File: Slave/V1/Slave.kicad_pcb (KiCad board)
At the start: 2 copper layers, 519 parts, among them J1301 649002227222, J1701 649002227222, J201 Header_Male_Pin_2.54mm_1X6_,_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, J202 Header_Male_Pin_2.54mm_1X3_,_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, J2101 649002227222, J2501 649002227222, J2901 649002227222, J300 Header_Male_Pin_2.54mm_1X2_,_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, J301 Header_Male_Pin_2.54mm_1X2_,_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, J3301 649002227222, J401 649006227222, J402 649006227222, J501 649002227222, J901 649002227222, Q1201 CPH6347-TL-W, Q1202 BSS806NH6327XTSA1, Q1301 CPH6347-TL-W, Q1302 CPH6347-TL-W, Q1601 CPH6347-TL-W, Q1602 BSS806NH6327XTSA1, Q1701 CPH6347-TL-W, Q1702 CPH6347-TL-W, Q2001 CPH6347-TL-W, Q2002 BSS806NH6327XTSA1, Q2101 CPH6347-TL-W, Q2102 CPH6347-TL-W, Q2401 CPH6347-TL-W, Q2402 BSS806NH6327XTSA1, Q2501 CPH6347-TL-W, Q2502 CPH6347-TL-W, Q2801 CPH6347-TL-W, Q2802 BSS806NH6327XTSA1, Q2901 CPH6347-TL-W, Q2902 CPH6347-TL-W, Q3201 CPH6347-TL-W, Q3202 BSS806NH6327XTSA1, Q3301 CPH6347-TL-W, Q3302 CPH6347-TL-W, Q3601 CPH6347-TL-W, Q3602 BSS806NH6327XTSA1, Q501 CPH6347-TL-W, Q502 CPH6347-TL-W, Q801 CPH6347-TL-W, Q802 BSS806NH6327XTSA1, Q901 CPH6347-TL-W, Q902 CPH6347-TL-W, SW201 PTS645SM43SMTR92, SW202 PTS645SM43SMTR92, U1001 AP3015KTR-G1, U1002 AP2202K-ADJTRG1, U1101 ADC121S021CIMF/NOPB, U1201 ADCMP350YKSZ-REEL7, U1301 LTV-816S, U1302 SI8641AB-B-IS1, U1401 AP3015KTR-G1, U1402 AP2202K-ADJTRG1, U1501 ADC121S021CIMF/NOPB, U1601 ADCMP350YKSZ-REEL7, U1701 LTV-816S, U1702 SI8641AB-B-IS1, U1801 AP3015KTR-G1, U1802 AP2202K-ADJTRG1, U1901 ADC121S021CIMF/NOPB, U2001 ADCMP350YKSZ-REEL7, U201 STM32F446RE, U2101 LTV-816S, U2102 SI8641AB-B-IS1, U2201 AP3015KTR-G1, U2202 AP2202K-ADJTRG1, U2301 ADC121S021CIMF/NOPB, U2401 ADCMP350YKSZ-REEL7, U2501 LTV-816S, U2502 SI8641AB-B-IS1, U2601 AP3015KTR-G1, U2602 AP2202K-ADJTRG1, U2701 ADC121S021CIMF/NOPB, U2801 ADCMP350YKSZ-REEL7, U2901 LTV-816S, U2902 SI8641AB-B-IS1, U3001 AP3015KTR-G1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

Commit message: Routing signals
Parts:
- removed J301: Header_Male_Pin_2.54mm_1X2_,_Unshrouded, Connectors:Headers_2.54mm_1X2
- removed TP201, TP202, TP203, TP302, TP304: Test_Point_THM, Connectors:Keystone_5001
- added F1301: 39511000440, Fuses:TE5_395, F.Cu at (98.8, 93.0)
- added F1701: 39511000440, Fuses:TE5_395, F.Cu at (98.8, 115.1)
- added F2101: 39511000440, Fuses:TE5_395, F.Cu at (208.0, 128.8)
- added F2501: 39511000440, Fuses:TE5_395, F.Cu at (208.0, 106.7)
- added F2901: 39511000440, Fuses:TE5_395, F.Cu at (208.0, 84.6)
- added F3301: 39511000440, Fuses:TE5_395, F.Cu at (208.0, 62.5)
- added F501: 39511000440, Fuses:TE5_395, F.Cu at (98.8, 48.8)
- added F901: 39511000440, Fuses:TE5_395, F.Cu at (98.8, 70.9)
- added J101: 649002227222, Connectors:649002227222, F.Cu at (211.6, 138.7)
- added J102: 649002227222, Connectors:649002227222, F.Cu at (95.5, 138.9)
- added Q101: 2N7002P,215, IC:SOT-23-3, F.Cu at (-0.57, -0.08)
- added R101: RC0805JR-07470RL, Resistors:R0805, F.Cu at (-1.80, -5.84)
- added R405: RC0805JR-07100RL, Resistors:R0805, F.Cu at (193.8, 148.1)
- C203, C204, C207, C208, C209, C210, C211, C212, C213, C301, C302, C303, C304, C404, D401, D402, R203, R204, R301, R302, R303, R402, R403, R404: moved to B.Cu
- C402, C403, C406, C407: value Capacitor_Generic -> 885012007053; moved to B.Cu
- C405: value Capacitor_Generic -> 885012207080
- R1310, R1710, R2110, R2510, R2910, R3310, R510, R910: moved to F.Cu
- R401: value Resistor_Generic -> RC0805JR-07100RL
- moved R401 355.4 mm to (204.7, 146.0), turned to 270 degrees
- moved C406 346.3 mm to (212.9, 165.6), turned to 180 degrees
- moved C407 339.8 mm to (216.7, 159.3), turned to 90 degrees
- moved C405 337.4 mm to (207.3, 146.0), turned to 270 degrees
- moved R303 336.5 mm to (180.1, 169.7), turned to 180 degrees
- moved D303 334.7 mm to (178.0, 169.7)
- moved D402 329.3 mm to (213.1, 152.9), turned to 180 degrees
- moved C402 328.6 mm to (195.6, 159.3), turned to 90 degrees
- moved C404 326.4 mm to (200.7, 145.3), turned to 180 degrees
- moved D302 324.1 mm to (171.2, 154.9), turned to 180 degrees
- moved TP401 321.5 mm to (201.2, 163.3), turned to 270 degrees
- moved C301 320.6 mm to (174.2, 163.8), turned to 270 degrees
- moved TP402 320.1 mm to (205.0, 150.1)
- moved D301 319.8 mm to (176.8, 154.9), turned to 180 degrees
- moved R402 319.7 mm to (201.2, 156.2), turned to 180 degrees
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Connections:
- C1302 pad 1: /Module 3/AVDD -> VDD
- C1302 pad 2: /Module 3/AGND -> DGND
- C1303 pad 1: /Module 3/AGND -> DGND
- C1702 pad 1: /Module 4/AVDD -> VDD
- C1702 pad 2: /Module 4/AGND -> DGND
- C1703 pad 1: /Module 4/AGND -> DGND
- C2102 pad 1: /Module 5/AVDD -> VDD
- C2102 pad 2: /Module 5/AGND -> DGND
- C2103 pad 1: /Module 5/AGND -> DGND
- C2502 pad 1: /Module 6/AVDD -> VDD
- C2502 pad 2: /Module 6/AGND -> DGND
- C2503 pad 1: /Module 6/AGND -> DGND
- C2902 pad 1: /Module 7/AVDD -> VDD
- C2902 pad 2: /Module 7/AGND -> DGND
- C2903 pad 1: /Module 7/AGND -> DGND
- C303 pad 2: Net-(C303-Pad2) -> 5V
- C3302 pad 1: /Module 8/AVDD -> VDD
- C3302 pad 2: /Module 8/AGND -> DGND
- C3303 pad 1: /Module 8/AGND -> DGND
- C502 pad 1: /Module 1/AVDD -> VDD
- C502 pad 2: /Module 1/AGND -> DGND
- C503 pad 1: /Module 1/AGND -> DGND
- C902 pad 1: /Module 2/AVDD -> VDD
- C902 pad 2: /Module 2/AGND -> DGND
- C903 pad 1: /Module 2/AGND -> DGND
- D402 pad 1: /CAN1/CAN_N -> /CAN1/CAN_P
- D402 pad 2: /CAN1/CAN_P -> /CAN1/CAN_N
- J1301 pad 2: /Module 3/CELL+ -> Net-(F1301-Pad1)
- J1701 pad 2: /Module 4/CELL+ -> Net-(F1701-Pad1)
- J2101 pad 2: /Module 5/CELL+ -> Net-(F2101-Pad1)
- J2501 pad 2: /Module 6/CELL+ -> Net-(F2501-Pad1)
- J2901 pad 2: /Module 7/CELL+ -> Net-(F2901-Pad1)
- J300 pad 1: Net-(C303-Pad2) -> 3.3V
- J300 pad 2: 5V -> VDD
- J3301 pad 2: /Module 8/CELL+ -> Net-(F3301-Pad1)
- J501 pad 2: /Module 1/CELL+ -> Net-(F501-Pad1)
- J901 pad 2: /Module 2/CELL+ -> Net-(F901-Pad1)
- R1303 pad 2: /Module 3/PWR_ENABLE -> VDD
- R1304 pad 2: /Module 3/BALANCING_PWM -> /BALANCING_PWM_3
- R1306 pad 2: /Module 3/CS_MCU -> /CS_3
- R1308 pad 2: /Module 3/SCLK_MCU -> /SCLK
- R1310 pad 2: /Module 3/SDATA_MCU -> /MISO
- R1311 pad 2: /Module 3/DATA_ENABLE -> /DATA_ENABLE_3
- R1314 pad 1: /Module 3/AGND -> DGND
- R1703 pad 2: /Module 4/PWR_ENABLE -> VDD
- R1704 pad 2: /Module 4/BALANCING_PWM -> /BALANCING_PWM_4
- R1706 pad 2: /Module 4/CS_MCU -> /CS_4
- R1708 pad 2: /Module 4/SCLK_MCU -> /SCLK
- R1710 pad 2: /Module 4/SDATA_MCU -> /MISO
- R1711 pad 2: /Module 4/DATA_ENABLE -> /DATA_ENABLE_4
- R1714 pad 1: /Module 4/AGND -> DGND
- R2103 pad 2: /Module 5/PWR_ENABLE -> VDD
- R2104 pad 2: /Module 5/BALANCING_PWM -> /BALANCING_PWM_5
- R2106 pad 2: /Module 5/CS_MCU -> /CS_5
- R2108 pad 2: /Module 5/SCLK_MCU -> /SCLK
- R2110 pad 2: /Module 5/SDATA_MCU -> /MISO
- R2111 pad 2: /Module 5/DATA_ENABLE -> /DATA_ENABLE_5
- R2114 pad 1: /Module 5/AGND -> DGND
- R2503 pad 2: /Module 6/PWR_ENABLE -> VDD
- R2504 pad 2: /Module 6/BALANCING_PWM -> /BALANCING_PWM_6
- R2506 pad 2: /Module 6/CS_MCU -> /CS_6
- R2508 pad 2: /Module 6/SCLK_MCU -> /SCLK
- R2510 pad 2: /Module 6/SDATA_MCU -> /MISO
- R2511 pad 2: /Module 6/DATA_ENABLE -> /DATA_ENABLE_6
- R2514 pad 1: /Module 6/AGND -> DGND
- R2903 pad 2: /Module 7/PWR_ENABLE -> VDD
- R2904 pad 2: /Module 7/BALANCING_PWM -> /BALANCING_PWM_7
- R2906 pad 2: /Module 7/CS_MCU -> /CS_7
- R2908 pad 2: /Module 7/SCLK_MCU -> /SCLK
- R2910 pad 2: /Module 7/SDATA_MCU -> /MISO
- R2911 pad 2: /Module 7/DATA_ENABLE -> /DATA_ENABLE_7
- R2914 pad 1: /Module 7/AGND -> DGND
- R302 pad 2: Net-(C303-Pad2) -> 5V
- R3303 pad 2: /Module 8/PWR_ENABLE -> VDD
- R3304 pad 2: /Module 8/BALANCING_PWM -> /BALANCING_PWM_8
- R3306 pad 2: /Module 8/CS_MCU -> /CS_8
- R3308 pad 2: /Module 8/SCLK_MCU -> /SCLK
- R3310 pad 2: /Module 8/SDATA_MCU -> /MISO
- R3311 pad 2: /Module 8/DATA_ENABLE -> /DATA_ENABLE_8
- R3314 pad 1: /Module 8/AGND -> DGND
- R503 pad 2: /Module 1/PWR_ENABLE -> VDD
- R504 pad 2: /Module 1/BALANCING_PWM -> /BALANCING_PWM_1
- R506 pad 2: /Module 1/CS_MCU -> /CS_1
- R508 pad 2: /Module 1/SCLK_MCU -> /SCLK
- R510 pad 2: /Module 1/SDATA_MCU -> /MISO
- R511 pad 2: /Module 1/DATA_ENABLE -> /DATA_ENABLE_1
- R514 pad 1: /Module 1/AGND -> DGND
- R903 pad 2: /Module 2/PWR_ENABLE -> VDD
- R904 pad 2: /Module 2/BALANCING_PWM -> /BALANCING_PWM_2
- R906 pad 2: /Module 2/CS_MCU -> /CS_2
- R908 pad 2: /Module 2/SCLK_MCU -> /SCLK
- R910 pad 2: /Module 2/SDATA_MCU -> /MISO
- R911 pad 2: /Module 2/DATA_ENABLE -> /DATA_ENABLE_2
- R914 pad 1: /Module 2/AGND -> DGND
- U1301 pad 2: /Module 3/AGND -> /PWR_ENABLE
- U1302 pad 1: /Module 3/AVDD -> VDD
- U1302 pad 2: /Module 3/AGND -> DGND
- U1302 pad 8: /Module 3/AGND -> DGND
- U1701 pad 2: /Module 4/AGND -> /PWR_ENABLE
- U1702 pad 1: /Module 4/AVDD -> VDD
- U1702 pad 2: /Module 4/AGND -> DGND
- U1702 pad 8: /Module 4/AGND -> DGND
- U201 pad 10: /PC2 -> /DATA_ENABLE_4
- U201 pad 11: /PC3 -> /CS_4
- U201 pad 28: /PB2 -> /CS_5
- U201 pad 29: /PB10 -> /DATA_ENABLE_5
- U201 pad 33: /PB12 -> /CS_6
- U201 pad 34: /PB13 -> /DATA_ENABLE_6
- U201 pad 35: /PB14 -> /CS_7
- U201 pad 36: /PB15 -> /DATA_ENABLE_7
- U201 pad 37: /PC6 -> /BALANCING_PWM_5
- U201 pad 38: /PC7 -> /BALANCING_PWM_6
- U201 pad 39: /PC8 -> /BALANCING_PWM_7
- U201 pad 40: /PC9 -> /BALANCING_PWM_8
- U201 pad 42: /PA9 -> /DATA_ENABLE_8
- U201 pad 43: /PA10 -> /CS_8
- U201 pad 50: /PA15 -> /DATA_ENABLE_1
- U201 pad 51: /PC10 -> /SCLK
- U201 pad 52: /PC11 -> /MISO
- U201 pad 53: /PC12 -> /CS_1
- U201 pad 54: /PD2 -> /DATA_ENABLE_2
- U201 pad 56: /PB4 -> /CS_2
- U201 pad 57: /PB5 -> /PWR_ENABLE_GPIO
- U201 pad 58: /PB6 -> /BALANCING_PWM_1
- U201 pad 59: /PB7 -> /BALANCING_PWM_2
- U201 pad 61: /PB8 -> /BALANCING_PWM_3
- U201 pad 62: /PB9 -> /BALANCING_PWM_4
- U201 pad 8: /PC0 -> /DATA_ENABLE_3
- U201 pad 9: /PC1 -> /CS_3
- U2101 pad 2: /Module 5/AGND -> /PWR_ENABLE
- U2102 pad 1: /Module 5/AVDD -> VDD
- U2102 pad 2: /Module 5/AGND -> DGND
- U2102 pad 8: /Module 5/AGND -> DGND
- U2501 pad 2: /Module 6/AGND -> /PWR_ENABLE
- U2502 pad 1: /Module 6/AVDD -> VDD
- U2502 pad 2: /Module 6/AGND -> DGND
- U2502 pad 8: /Module 6/AGND -> DGND
- U2901 pad 2: /Module 7/AGND -> /PWR_ENABLE
- U2902 pad 1: /Module 7/AVDD -> VDD
- U2902 pad 2: /Module 7/AGND -> DGND
- U2902 pad 8: /Module 7/AGND -> DGND
- U301 pad 3: Net-(C303-Pad2) -> 5V
- U3301 pad 2: /Module 8/AGND -> /PWR_ENABLE
- U3302 pad 1: /Module 8/AVDD -> VDD
- U3302 pad 2: /Module 8/AGND -> DGND
- U3302 pad 8: /Module 8/AGND -> DGND
- U401 pad 4: /PA11 -> Net-(R405-Pad2)
- U501 pad 2: /Module 1/AGND -> /PWR_ENABLE
- U502 pad 1: /Module 1/AVDD -> VDD
- U502 pad 2: /Module 1/AGND -> DGND
- U502 pad 8: /Module 1/AGND -> DGND
- U901 pad 2: /Module 2/AGND -> /PWR_ENABLE
- U902 pad 1: /Module 2/AVDD -> VDD
- U902 pad 2: /Module 2/AGND -> DGND
- U902 pad 8: /Module 2/AGND -> DGND
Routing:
- net VDD: track 0.00 -> 289.2 mm, vias 0 -> 18
- net DGND: track 0.00 -> 280.9 mm, vias 0 -> 22
- net /SCLK: track 0.00 -> 160.2 mm, vias 0 -> 8
- net /MISO: track 0.00 -> 98.7 mm
- net /PWR_ENABLE: track 0.00 -> 98.2 mm, vias 0 -> 4
- net /DATA_ENABLE_4: track 0.00 -> 97.5 mm, vias 0 -> 2
- net /CS_4: track 0.00 -> 96.9 mm, vias 0 -> 2
- net /BALANCING_PWM_8: track 0.00 -> 83.0 mm, vias 0 -> 1
- net /DATA_ENABLE_1: track 0.00 -> 81.5 mm, vias 0 -> 1
- net /CS_8: track 0.00 -> 81.4 mm
- net /DATA_ENABLE_3: track 0.00 -> 80.7 mm, vias 0 -> 1
- net /BALANCING_PWM_1: track 0.00 -> 79.6 mm, vias 0 -> 1
- net /CS_1: track 0.00 -> 79.4 mm, vias 0 -> 2
- net /DATA_ENABLE_8: track 0.00 -> 77.7 mm, vias 0 -> 1
- net /CS_3: track 0.00 -> 75.6 mm, vias 0 -> 2
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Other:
- net class Default: clearance 0.254 -> 0.2032; trace_width 0.254 -> 0.2032
- rule trace_clearance: 0.254 -> 0.2032
- board text added: "12V"
- board text added: "3.3V"
- board text added: "5V"
- board text added: "DGND"
- board text added: "RESET"
- board text added: "USER"

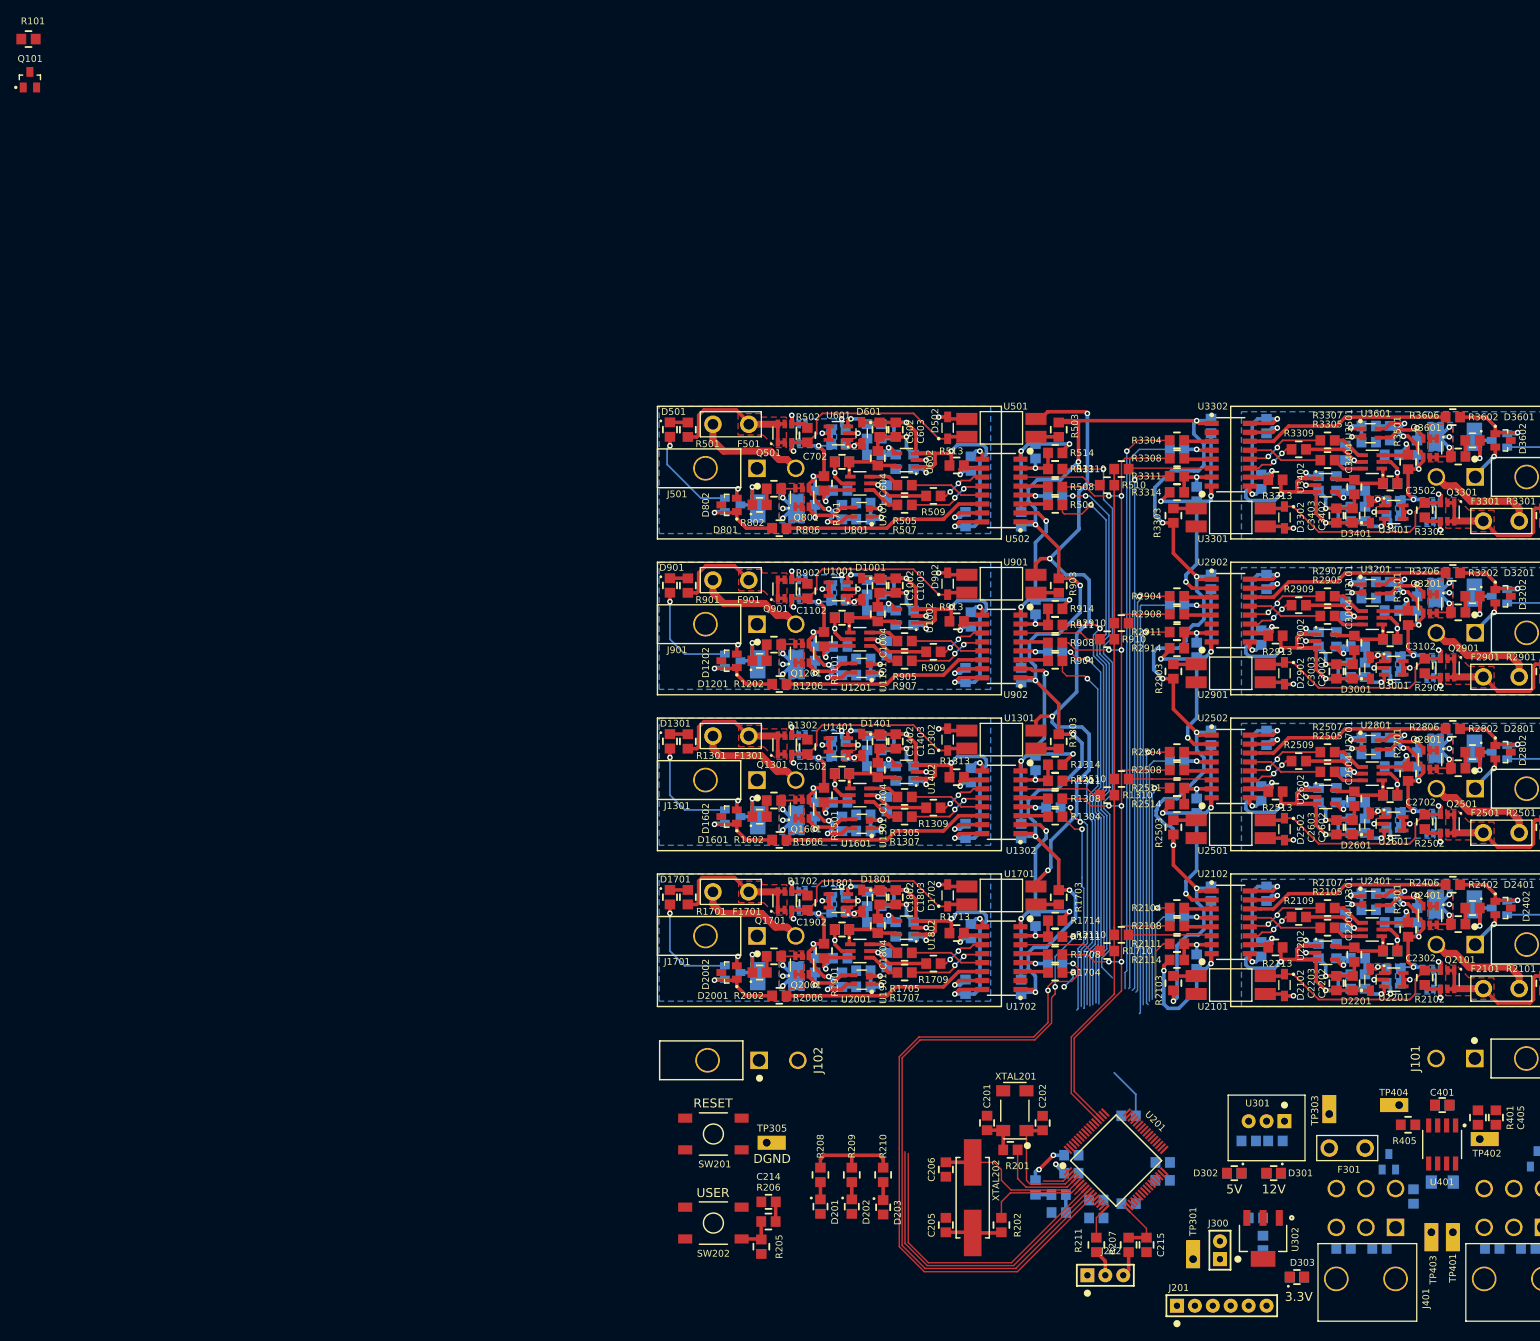
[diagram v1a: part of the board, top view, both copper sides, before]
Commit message: Routing signals 2
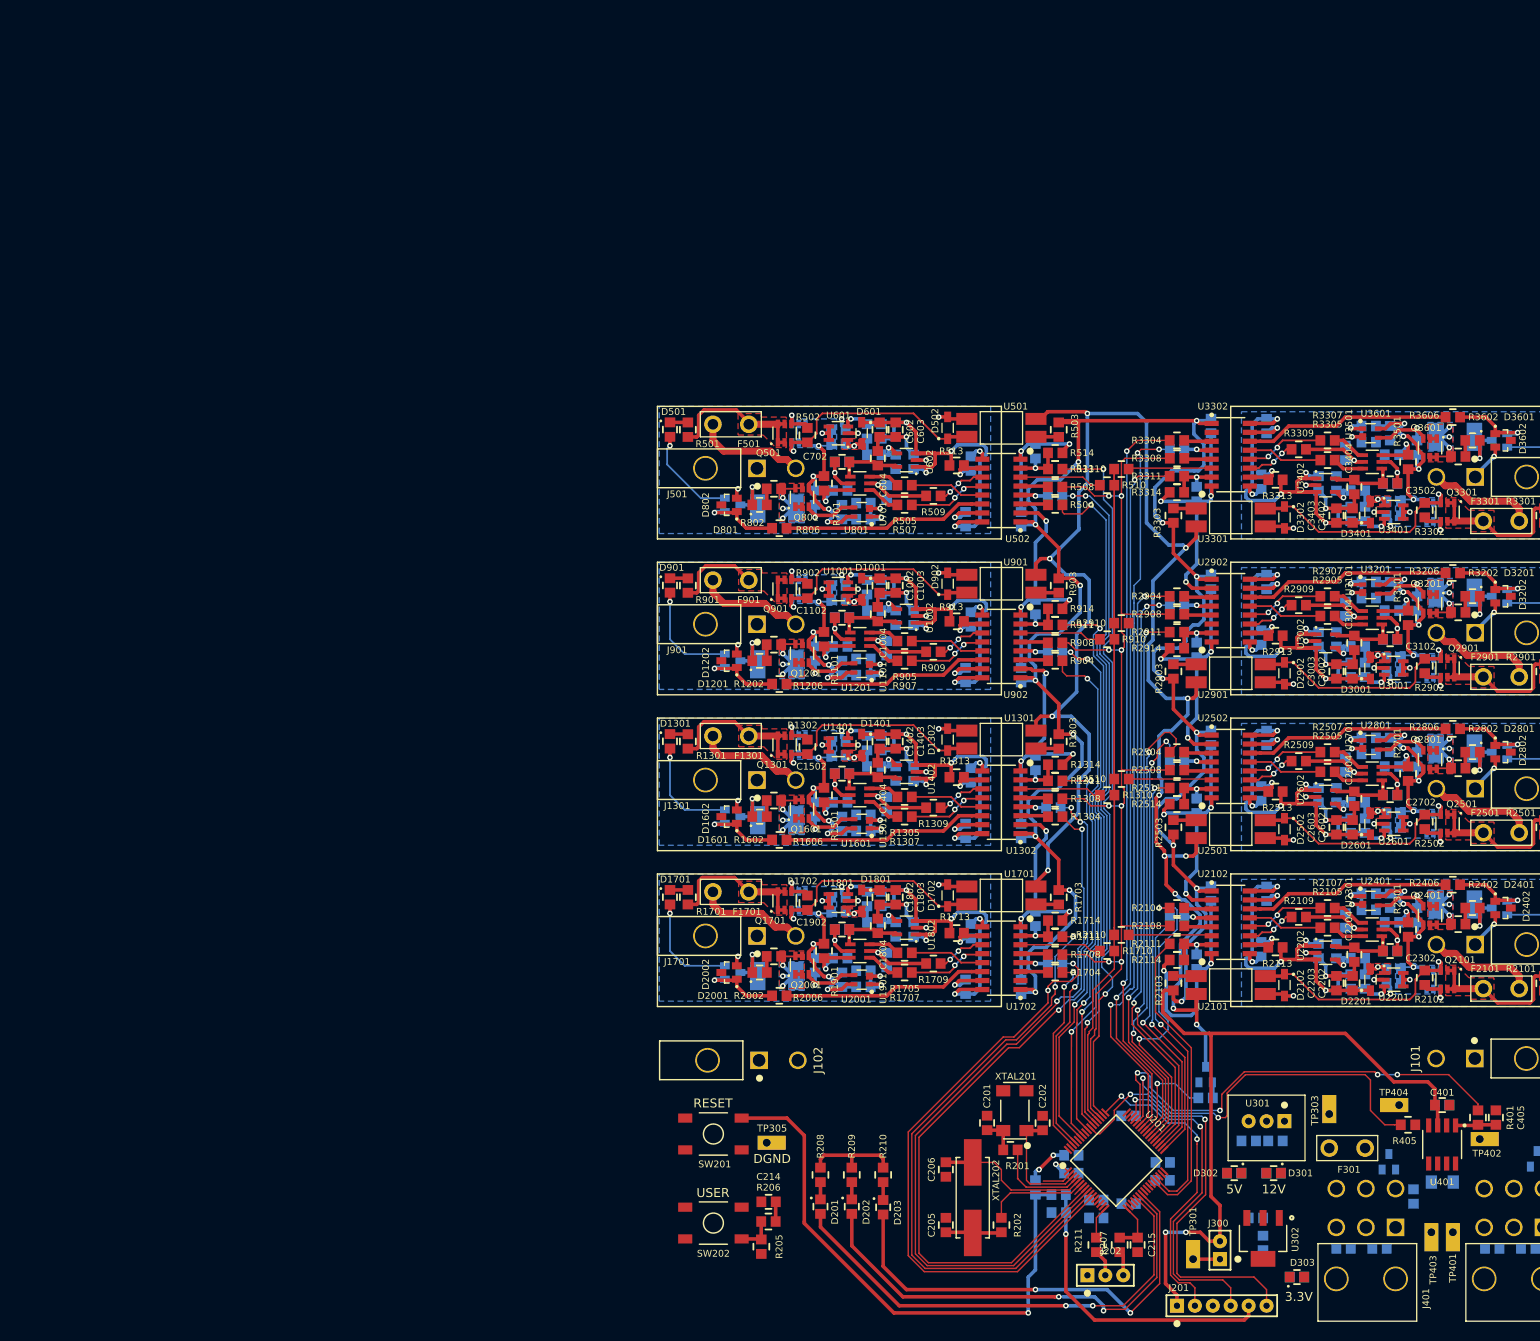
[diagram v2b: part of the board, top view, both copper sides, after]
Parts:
- Q101, R101: moved to B.Cu
- moved R101 226.0 mm to (167.1, 144.3), turned to 180 degrees
- moved Q101 218.4 mm to (166.1, 141.0), turned to 180 degrees
- moved C215 1.27 mm to (156.5, 166.1)
- moved R207 1.27 mm to (153.9, 166.1)
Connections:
- U201 pad 28: /CS_5 -> /DATA_ENABLE_5
- U201 pad 29: /DATA_ENABLE_5 -> /CS_5
- U201 pad 33: /CS_6 -> /DATA_ENABLE_6
- U201 pad 34: /DATA_ENABLE_6 -> /CS_6
- U201 pad 35: /CS_7 -> /DATA_ENABLE_7
- U201 pad 36: /DATA_ENABLE_7 -> /CS_7
- U201 pad 41: /PA8 -> /PWR_ENABLE_GPIO
- U201 pad 57: /PWR_ENABLE_GPIO -> /PB5
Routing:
- net /PWR_ENABLE: track 98.2 -> 236.9 mm, vias 4 -> 12
- net VDD: track 289.2 -> 390.9 mm, vias 18 -> 20
- net Net-(R203-Pad1): track 2.27 -> 78.8 mm, vias 0 -> 1
- net /PA5: track 0.00 -> 67.4 mm, vias 0 -> 2
- net /PA6: track 0.00 -> 66.5 mm, vias 0 -> 2
- net /PA12: track 0.00 -> 65.0 mm, vias 0 -> 4
- net /PA7: track 0.00 -> 64.8 mm, vias 0 -> 2
- net /STM32F446/SWO: track 0.00 -> 60.6 mm, vias 0 -> 2
- net /PA11: track 0.00 -> 56.0 mm, vias 0 -> 2
- net /STM32F446/SWDIO: track 0.00 -> 47.8 mm, vias 0 -> 2
- net /STM32F446/SWCLK: track 0.00 -> 44.4 mm, vias 0 -> 2
- net /BALANCING_PWM_5: track 1.77 -> 44.6 mm, vias 1 -> 2
- net /NRST: track 4.16 -> 44.6 mm, vias 0 -> 1
- net /DATA_ENABLE_5: track 8.98 -> 43.4 mm
- net /CS_5: track 12.8 -> 45.8 mm, vias 0 -> 1
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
